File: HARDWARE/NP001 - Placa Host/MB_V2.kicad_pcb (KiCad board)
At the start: 2 copper layers, 166.4 x 57.1 mm, 38 parts, among them J10 GPS/GPRS, J11 TP_RX_PIC, J12 TP_SDO, J13 TP_SCK, J14 DM3CS-SF, J15 Sensor_SO2, J16 Sensor_O3, J17 Sensor_NO2, J18 Sensor_PM10, J2 Datos_LORA, J3 Salida_Bomba, J4 Sensor_CO, J5 POWER_MB, J6 TP_SCL, J7 PICKIT3, J8 TP_SDA, J9 TP_TX_PIC, Q1 BC807, U1 AP1117-33, U3 PIC24FJ64GB002-I/P, Y1 8MHz

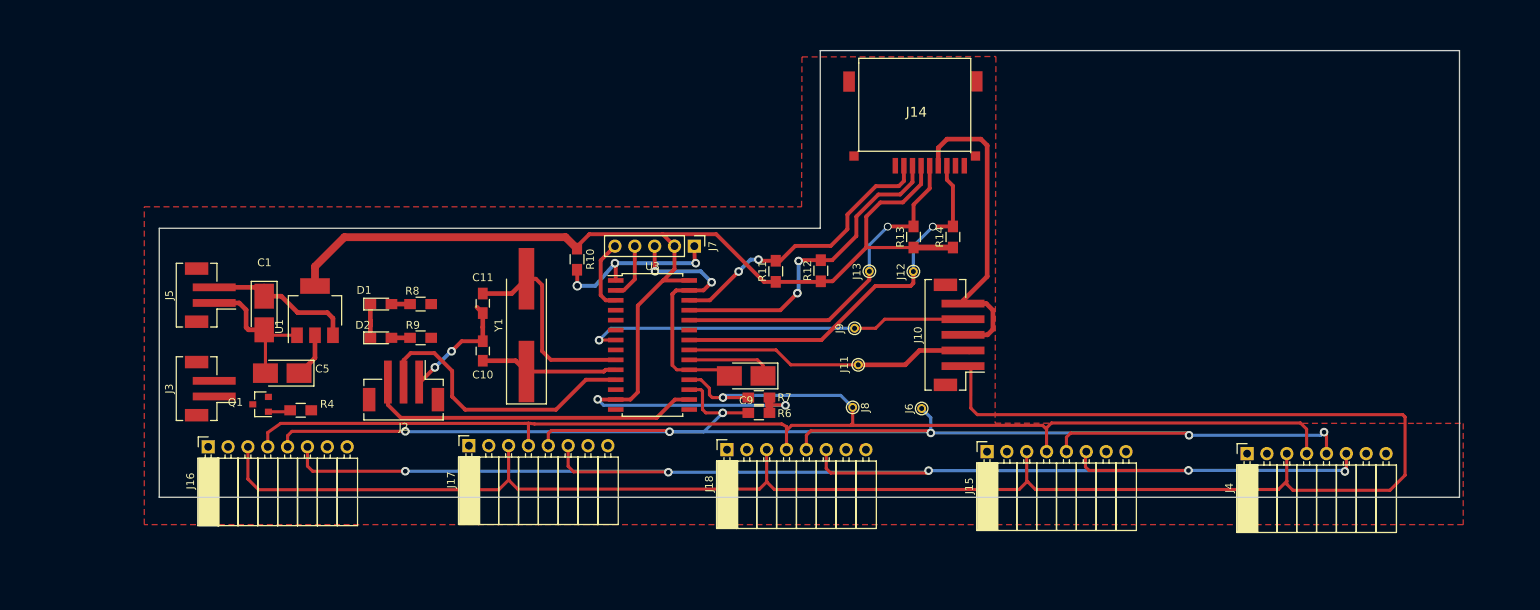
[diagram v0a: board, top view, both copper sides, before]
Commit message: 
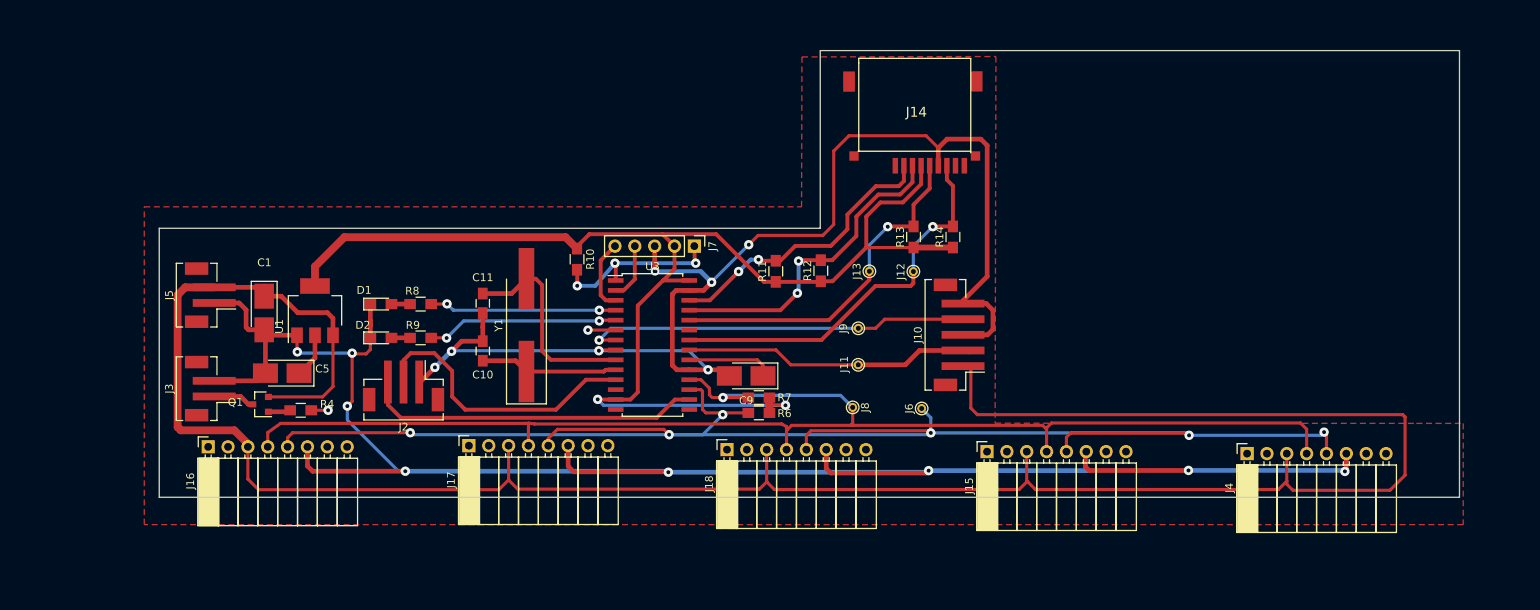
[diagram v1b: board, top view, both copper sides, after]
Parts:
- moved J9 0.48 mm to (144.1, 114.4)
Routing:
- net GND: track 299.6 -> 416.8 mm, vias 9 -> 15
- net VDD2: track 262.3 -> 309.9 mm
- net Net-(R9-Pad1): track 0.00 -> 24.6 mm, vias 0 -> 2
- net Net-(R8-Pad1): track 1.09 -> 25.1 mm, vias 0 -> 2
- net Bomba: track 1.25 -> 7.03 mm, vias 0 -> 2
- net V_Bomba: track 0.05 -> 5.40 mm
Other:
- net class Default: clearance 0.2 -> 0.1
- net class VDD: clearance 0.2 -> 0.1
- net class uC: clearance 0.2 -> 0.1
- rule trace_clearance: 0.2 -> 0.1

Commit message: Daniel Prieto:
-Subo placa enviada a China.
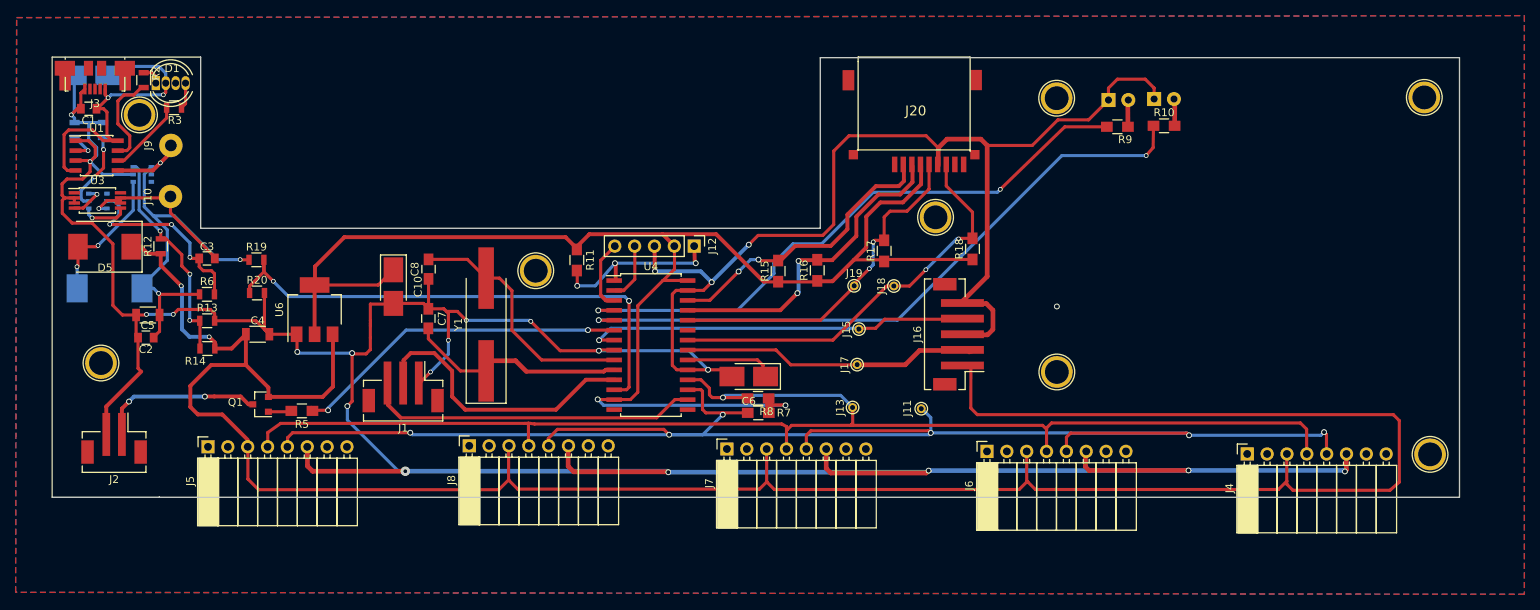
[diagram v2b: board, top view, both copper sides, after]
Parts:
- removed C11: 33pF, Capacitors_SMD:C_0805_HandSoldering
- removed D2: LED, LEDs:LED_0805_HandSoldering
- removed J14: DM3CS-SF, SD_CARD_DP:SD_CARD_DP
- added ?: 1pin, Connectors:1pin, F.Cu at (154.0, 100.2)
- added ?: 1pin, Connectors:1pin, F.Cu at (52.2, 87.1)
- added ?: 1pin, Connectors:1pin, F.Cu at (216.6, 84.8)
- added ?: 1pin, Connectors:1pin, F.Cu at (217.3, 130.5)
- added ?: 1pin, Connectors:1pin, F.Cu at (169.5, 120.0)
- added ?: 1pin, Connectors:1pin, F.Cu at (169.5, 84.9)
- added ?: 1pin, Connectors:1pin, F.Cu at (47.2, 118.8)
- added ?: 1pin, Connectors:1pin, F.Cu at (102.9, 107.0)
- added C2: 10u, Capacitors_SMD:C_0805, F.Cu at (53.0, 115.6)
- added C3: 0.1u, Capacitors_SMD:C_0805, F.Cu at (60.8, 105.4)
- added C4: 28u, Capacitors_SMD:C_1206, F.Cu at (67.3, 115.1)
- added C6: 10uF, Capacitors_Tantalum_SMD:CP_Tantalum_Case-B_EIA-3528-21_Hand, F.Cu at (130.1, 120.5)
- added C7: 33pF, Capacitors_SMD:C_0805_HandSoldering, F.Cu at (89.1, 113.1)
- added C8: 33pF, Capacitors_SMD:C_0805_HandSoldering, F.Cu at (89.2, 106.8)
- added D3: LED, LEDs:LED_D3.0mm_Horizontal_O1.27mm_Z2.0mm, B.Cu at (176.1, 85.2)
- added D4: LED, LEDs:LED_D3.0mm_Horizontal_O1.27mm_Z2.0mm, B.Cu at (182.0, 85.0)
- added D5: SS34, Diodes_SMD:D_SMC, F.Cu at (47.7, 103.9)
- added J1: Datos_LORA, Connectors_JST:JST_PH_B3B-PH-SM4-TB_03x2.00mm_Straight, F.Cu at (85.9, 122.5)
- added J19: TP_SCK, Connectors:PINTST, F.Cu at (143.6, 108.9)
- added J20: DM3CS-SF, SD_CARD_DP:SD_CARD_DP, F.Cu at (151.1, 85.8)
- added L1: 22u, Inductors_SMD:L_10.4x10.4_H4.8, B.Cu at (48.3, 109.3)
- added R1: 1.2k, Resistors_SMD:R_0805, B.Cu at (43.9, 89.0)
- added R15: 4.7K, Resistors_SMD:R_0805_HandSoldering, F.Cu at (133.9, 107.1)
- added R16: 4.7K, Resistors_SMD:R_0805_HandSoldering, F.Cu at (138.9, 107.0)
- added R17: 4.7K, Resistors_SMD:R_0805_HandSoldering, F.Cu at (147.4, 104.5)
- added R18: 4.7K, Resistors_SMD:R_0805_HandSoldering, F.Cu at (158.8, 104.2)
- added R19: R, Resistors_SMD:R_0805, F.Cu at (67.1, 105.6)
- added R2: 1k, Resistors_SMD:R_0805, F.Cu at (52.7, 82.6)
- added R20: R, Resistors_SMD:R_0805, F.Cu at (67.2, 109.9)
- added R3: 1k, Resistors_SMD:R_0805, F.Cu at (56.6, 86.2)
- added R5: 4.7K, Resistors_SMD:R_0805_HandSoldering, F.Cu at (72.9, 124.9)
- added U2: DW01-P, Housings_SSOP:TSOP-6_1.65x3.05mm_Pitch0.95mm, B.Cu at (46.8, 98.1)
- added U4: PIC24FJ64GB002-I/P, Housings_SOIC:SOIC-28W_7.5x17.9mm_Pitch1.27mm, F.Cu at (117.6, 116.5)
- added U5: MT3608, Housings_SSOP:TSOP-6_1.65x3.05mm_Pitch0.95mm, B.Cu at (52.5, 94.7)
- added U6: AP1117-33, TO_SOT_Packages_SMD:SOT-223-3_TabPin2, F.Cu at (74.6, 112.0)
- C1: value 0.1uF -> 0.1u; footprint Capacitors_Tantalum_SMD:CP_Tantalum_Case-B_EIA-3528-21_Hand -> Capacitors_SMD:C_0805
- C10: value 33pF -> 1uF; footprint Capacitors_SMD:C_0805_HandSoldering -> Capacitors_Tantalum_SMD:CP_Tantalum_Case-B_EIA-3528-21_Hand
- C5: value 1uF -> 28u; footprint Capacitors_Tantalum_SMD:CP_Tantalum_Case-B_EIA-3528-21_Hand -> Capacitors_SMD:C_1206
- C9: value 10uF -> 0.1uF; moved to B.Cu
- D1: value LED -> LED_RCGB; footprint LEDs:LED_0805_HandSoldering -> LEDs:LED_D5.0mm-4
- J10: value GPS/GPRS -> BAT-; footprint Connectors_JST:JST_PH_B5B-PH-SM4-TB_05x2.00mm_Straight -> Mounting_Holes:MountingHole_2.2mm_M2_DIN965_Pad
- J11: value TP_RX_PIC -> TP_SCL
- J12: value TP_SDO -> PICKIT3; footprint Connectors:PINTST -> Pin_Headers:Pin_Header_Straight_1x05_Pitch2.54mm
- J13: value TP_SCK -> TP_SDA
- J15: value Sensor_SO2 -> TP_TX_PIC; footprint Socket_Strips:Socket_Strip_Angled_1x08_Pitch2.54mm -> Connectors:PINTST
- J16: value Sensor_O3 -> GPS/GPRS; footprint Socket_Strips:Socket_Strip_Angled_1x08_Pitch2.54mm -> Connectors_JST:JST_PH_B5B-PH-SM4-TB_05x2.00mm_Straight
- J17: value Sensor_NO2 -> TP_RX_PIC; footprint Socket_Strips:Socket_Strip_Angled_1x08_Pitch2.54mm -> Connectors:PINTST
- J18: value Sensor_PM10 -> TP_SDO; footprint Socket_Strips:Socket_Strip_Angled_1x08_Pitch2.54mm -> Connectors:PINTST
- J2: value Datos_LORA -> Salida_Bomba; footprint Connectors_JST:JST_PH_B3B-PH-SM4-TB_03x2.00mm_Straight -> Connectors_JST:JST_PH_B2B-PH-SM4-TB_02x2.00mm_Straight
- J3: value Salida_Bomba -> Entrada_Alimentacion; footprint Connectors_JST:JST_PH_B2B-PH-SM4-TB_02x2.00mm_Straight -> Connectors_USB:USB_Micro-B_Molex_47346-0001
- J5: value POWER_MB -> Sensor_SO2; footprint Connectors_JST:JST_PH_B2B-PH-SM4-TB_02x2.00mm_Straight -> Socket_Strips:Socket_Strip_Angled_1x08_Pitch2.54mm
- J6: value TP_SCL -> Sensor_O3; footprint Connectors:PINTST -> Socket_Strips:Socket_Strip_Angled_1x08_Pitch2.54mm
- J7: value PICKIT3 -> Sensor_NO2; footprint Pin_Headers:Pin_Header_Straight_1x05_Pitch2.54mm -> Socket_Strips:Socket_Strip_Angled_1x08_Pitch2.54mm
- J8: value TP_SDA -> Sensor_PM10; footprint Connectors:PINTST -> Socket_Strips:Socket_Strip_Angled_1x08_Pitch2.54mm
- J9: value TP_TX_PIC -> BAT+; footprint Connectors:PINTST -> Mounting_Holes:MountingHole_2.2mm_M2_DIN965_Pad
- R10: value 4k7 -> 220
- R11: value 4.7K -> 4k7
- R12: value 4.7K -> 18k; footprint Resistors_SMD:R_0805_HandSoldering -> Resistors_SMD:R_0805
- R13: value 4.7K -> 2.2k; footprint Resistors_SMD:R_0805_HandSoldering -> Resistors_SMD:R_0805
- R14: value 4.7K -> 180k; footprint Resistors_SMD:R_0805_HandSoldering -> Resistors_SMD:R_0805
- R4: value 4.7K -> 1k; footprint Resistors_SMD:R_0805_HandSoldering -> Resistors_SMD:R_0805; moved to B.Cu
- R6: value 4.7K -> 100; footprint Resistors_SMD:R_0805_HandSoldering -> Resistors_SMD:R_0805
- R8: value 220 -> 4.7K
- U1: value AP1117-33 -> TP4056; footprint TO_SOT_Packages_SMD:SOT-223-3_TabPin2 -> Housings_SOIC:SOIC-8_3.9x4.9mm_Pitch1.27mm
- U3: value PIC24FJ64GB002-I/P -> 8205A; footprint Housings_SOIC:SOIC-28W_7.5x17.9mm_Pitch1.27mm -> Housings_SSOP:TSSOP-8_4.4x3mm_Pitch0.65mm
- moved J10 101.8 mm to (56.1, 97.5)
- moved J16 96.5 mm to (156.3, 115.1)
- moved R14 96.5 mm to (60.9, 117.0), turned to 180 degrees
- moved R9 93.2 mm to (177.3, 88.6), turned to 0 degrees
- moved C9 92.2 mm to (46.0, 82.0)
- moved J9 91.0 mm to (56.2, 91.0)
- moved R13 91.0 mm to (60.8, 113.4), turned to 0 degrees
- moved R12 84.5 mm to (54.9, 103.9)
- moved R10 77.0 mm to (183.3, 88.5), turned to 0 degrees
- moved U3 73.4 mm to (46.8, 98.0)
- moved R6 72.2 mm to (60.8, 110.0)
- moved J17 50.7 mm to (144.0, 119.0)
- moved J8 49.3 mm to (94.4, 129.4), turned to 90 degrees
- moved R8 44.8 mm to (131.3, 123.3), turned to 0 degrees
- moved R4 43.9 mm to (47.5, 89.0), turned to 90 degrees
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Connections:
- C1 pad 1: VDD2 -> +5V
- C10 pad 1: GND -> VDD1
- C10 pad 2: Net-(C10-Pad2) -> GND
- C5 pad 1: VDD1 -> BAT+
- C9 pad 1: Net-(C9-Pad1) -> +5V
- D1 pad 1: GND -> Net-(D1-Pad1)
- D1 pad 2: Net-(D1-Pad2) -> +5V
- J10 pad 1: VDD2 -> Net-(C3-Pad2)
- J11 pad 1: Net-(J10-Pad2) -> SCL
- J13 pad 1: Net-(J13-Pad1) -> SDA
- J15 pad 1: (no net) -> Net-(J15-Pad1)
- J16 pad 1: (no net) -> VDD2
- J16 pad 2: (no net) -> Net-(J16-Pad2)
- J16 pad 3: VDD2 -> GND
- J16 pad 4: SDA -> Net-(J15-Pad1)
- J16 pad 5: SCL -> GND
- J17 pad 1: (no net) -> Net-(J16-Pad2)
- J18 pad 1: (no net) -> Net-(J18-Pad1)
- J2 pad 1: GND -> V_Bomba
- J2 pad 2: LORA_UART_TX -> GND
- J3 pad 1: V_Bomba -> +5V
- J3 pad 2: GND -> (no net)
- J5 pad 1: GND -> (no net)
- J5 pad 2: VDD2 -> (no net)
- J6 pad 1: SCL -> (no net)
- J7 pad 1: Net-(J7-Pad1) -> (no net)
- J7 pad 2: VDD1 -> (no net)
- J7 pad 3: GND -> VDD2
- J7 pad 4: Net-(J7-Pad4) -> SDA
- J7 pad 5: Net-(J7-Pad5) -> SCL
- J8 pad 1: SDA -> (no net)
- J9 pad 1: Net-(J10-Pad4) -> BAT+
- R10 pad 1: VDD1 -> Net-(R10-Pad1)
- R10 pad 2: Net-(J7-Pad1) -> Net-(D4-Pad2)
- R11 pad 2: Net-(J14-Pad2) -> Net-(J12-Pad1)
- R12 pad 1: VDD1 -> VDD2
- R12 pad 2: Net-(J14-Pad3) -> Net-(R12-Pad2)
- R13 pad 1: VDD1 -> Net-(R12-Pad2)
- R13 pad 2: Net-(J13-Pad1) -> GND
- R14 pad 1: VDD1 -> VDD2
- R14 pad 2: Net-(J12-Pad1) -> Net-(R12-Pad2)
- R4 pad 1: Bomba -> Net-(R4-Pad1)
- R4 pad 2: Net-(Q1-Pad1) -> GND
- R6 pad 1: SCL -> BAT+
- R6 pad 2: VDD1 -> Net-(C3-Pad1)
- R7 pad 1: SDA -> SCL
- R8 pad 1: Net-(R8-Pad1) -> SDA
- R8 pad 2: Net-(D1-Pad2) -> VDD1
- U1 pad 2: VDD1 -> Net-(R1-Pad2)
- U1 pad 3: VDD2 -> GND
- U3 pad 1: Net-(J7-Pad1) -> (no net)
- U3 pad 2: Net-(J7-Pad4) -> GND
- U3 pad 3: Net-(J7-Pad5) -> GND
- U3 pad 4: Net-(R8-Pad1) -> Net-(U2-Pad3)
- U3 pad 5: Net-(R9-Pad1) -> Net-(U2-Pad1)
- U3 pad 6: Bomba -> Net-(C3-Pad2)
- U3 pad 7: Net-(J10-Pad4) -> Net-(C3-Pad2)
- U3 pad 8: GND -> (no net)
- Y1 pad 1: Net-(C10-Pad2) -> Net-(C7-Pad2)
- Y1 pad 2: Net-(C11-Pad2) -> Net-(C8-Pad2)
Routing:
- net GND: track 416.8 -> 541.6 mm, vias 15 -> 22
- net Net-(R10-Pad1): track 0.00 -> 84.9 mm, vias 0 -> 2
- net V_BAT: track 0.00 -> 67.9 mm, vias 0 -> 2
- net BAT+: track 0.00 -> 62.4 mm, vias 0 -> 3
- net Net-(J18-Pad1): track 0.00 -> 53.4 mm, vias 0 -> 2
- net Net-(R9-Pad1): track 24.6 -> 77.6 mm
- net Net-(J15-Pad1): track 0.00 -> 49.8 mm, vias 0 -> 2
- net Net-(J10-Pad4): track 49.8 -> 0.00 mm, vias 1 -> 0
- net Net-(J19-Pad1): track 0.00 -> 45.0 mm, vias 0 -> 2
- net Net-(J13-Pad1): track 45.0 -> 0.00 mm, vias 1 -> 0
- net +5V: track 0.00 -> 41.9 mm, vias 0 -> 2
- net Net-(J20-Pad3): track 0.00 -> 41.2 mm, vias 0 -> 2
- net Net-(J14-Pad3): track 41.2 -> 0.00 mm, vias 2 -> 0
- net Net-(J10-Pad2): track 37.8 -> 0.00 mm
- net Net-(J16-Pad2): track 0.00 -> 37.8 mm
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- added copper zone on B.Cu, net GND
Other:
- board size 166.4 x 57.1 mm -> 180.1 x 56.3 mm
